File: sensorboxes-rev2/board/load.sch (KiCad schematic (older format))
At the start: 26 parts

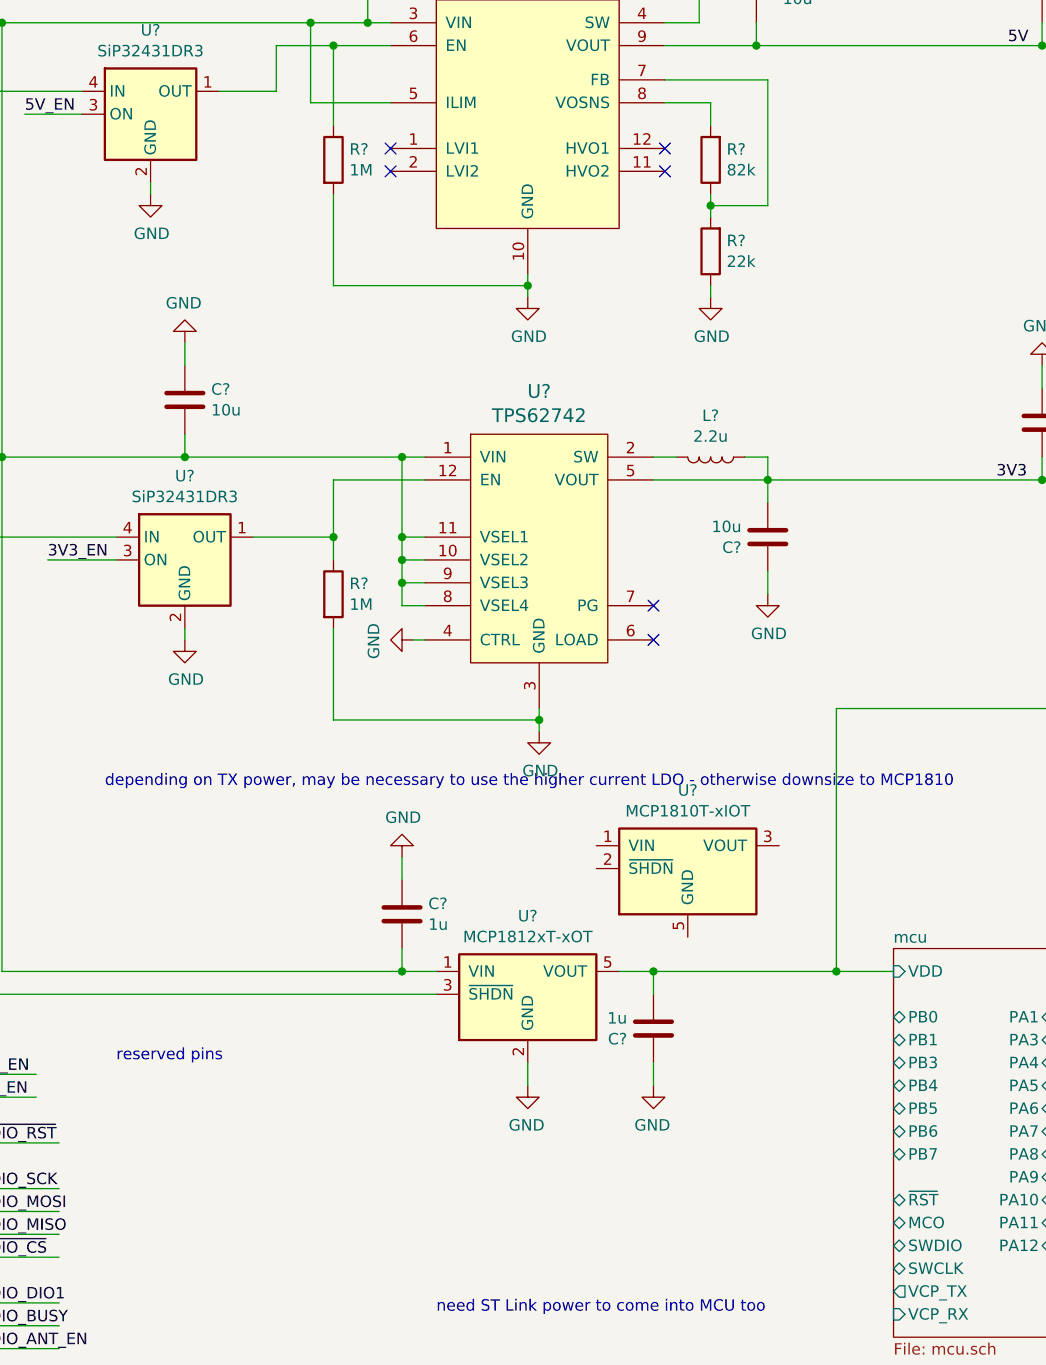
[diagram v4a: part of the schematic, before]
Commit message: exposing pins for mcu, added part values for RF section
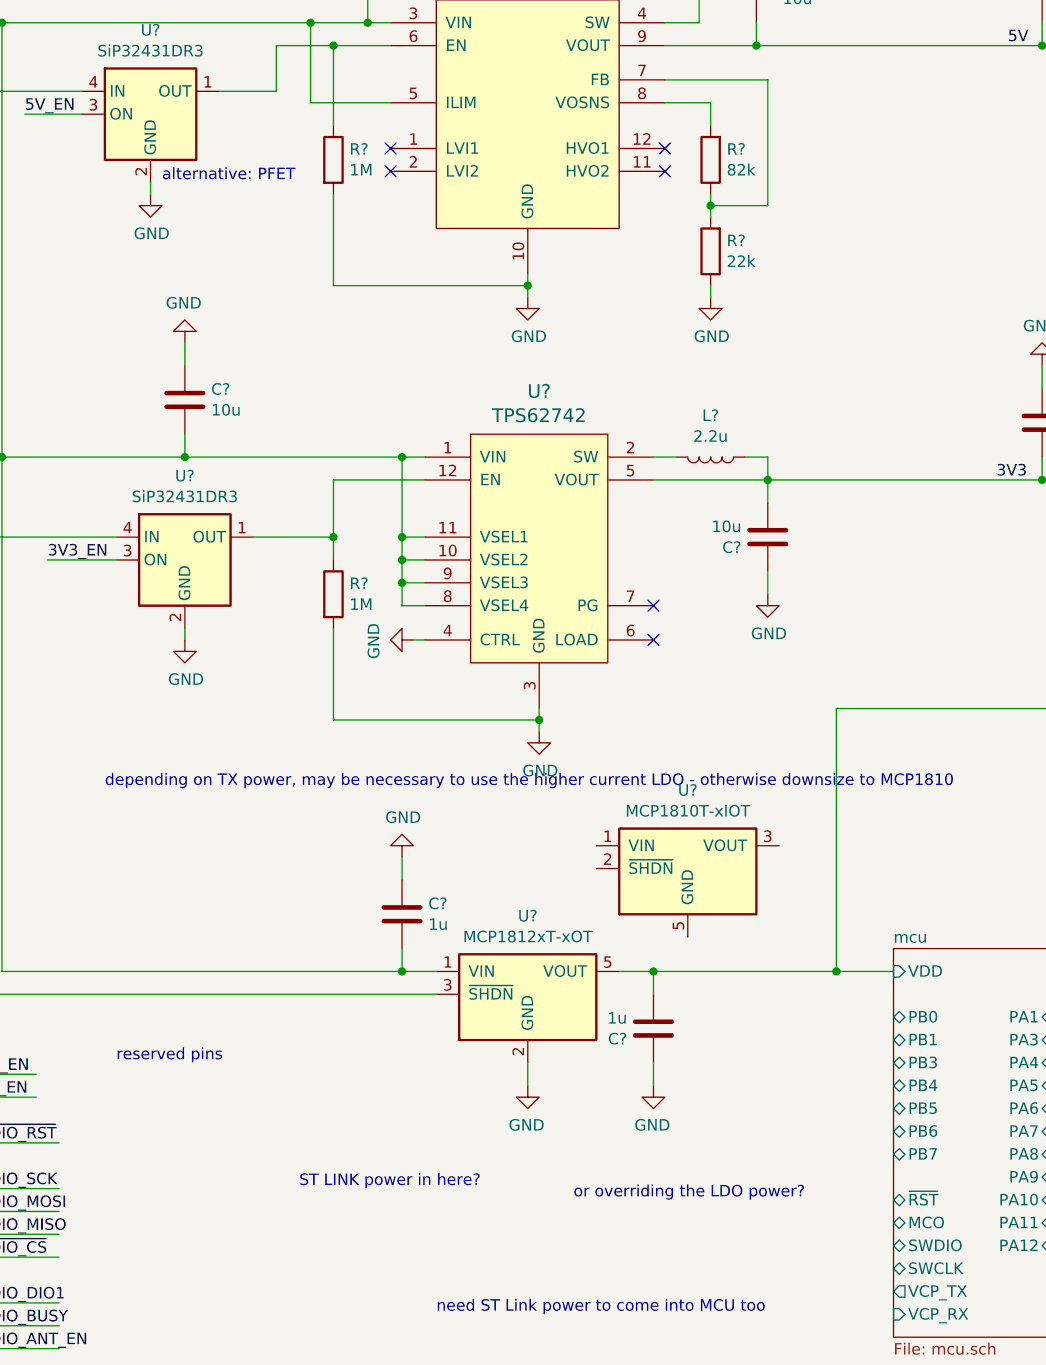
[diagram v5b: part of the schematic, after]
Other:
- note added: "ST LINK power in here?"
- note added: "alternative: PFET"
- note added: "or overriding the LDO power?"
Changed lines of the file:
@@
 Wire Wire Line
 	1300 7600 1700 7600
+Text Notes 2150 2500 0    50   ~ 0
+alternative: PFET
+Text Notes 2750 6900 0    50   ~ 0
+ST LINK power in here?
+Text Notes 3950 6950 0    50   ~ 0
+or overriding the LDO power?
 $EndSCHEMATC

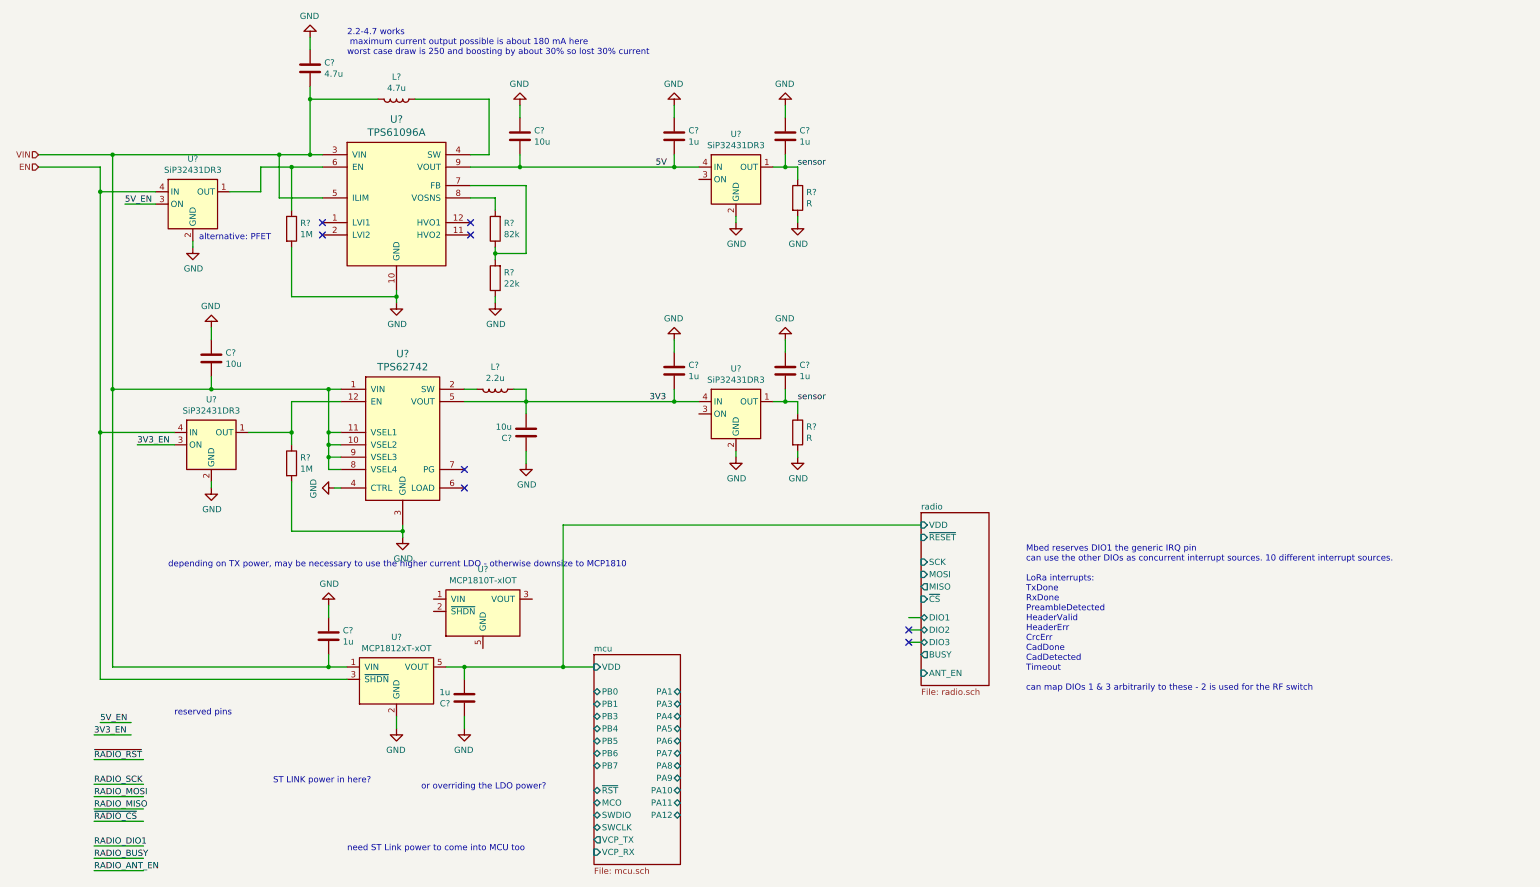
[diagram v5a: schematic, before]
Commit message: some preliminary power figure estimation
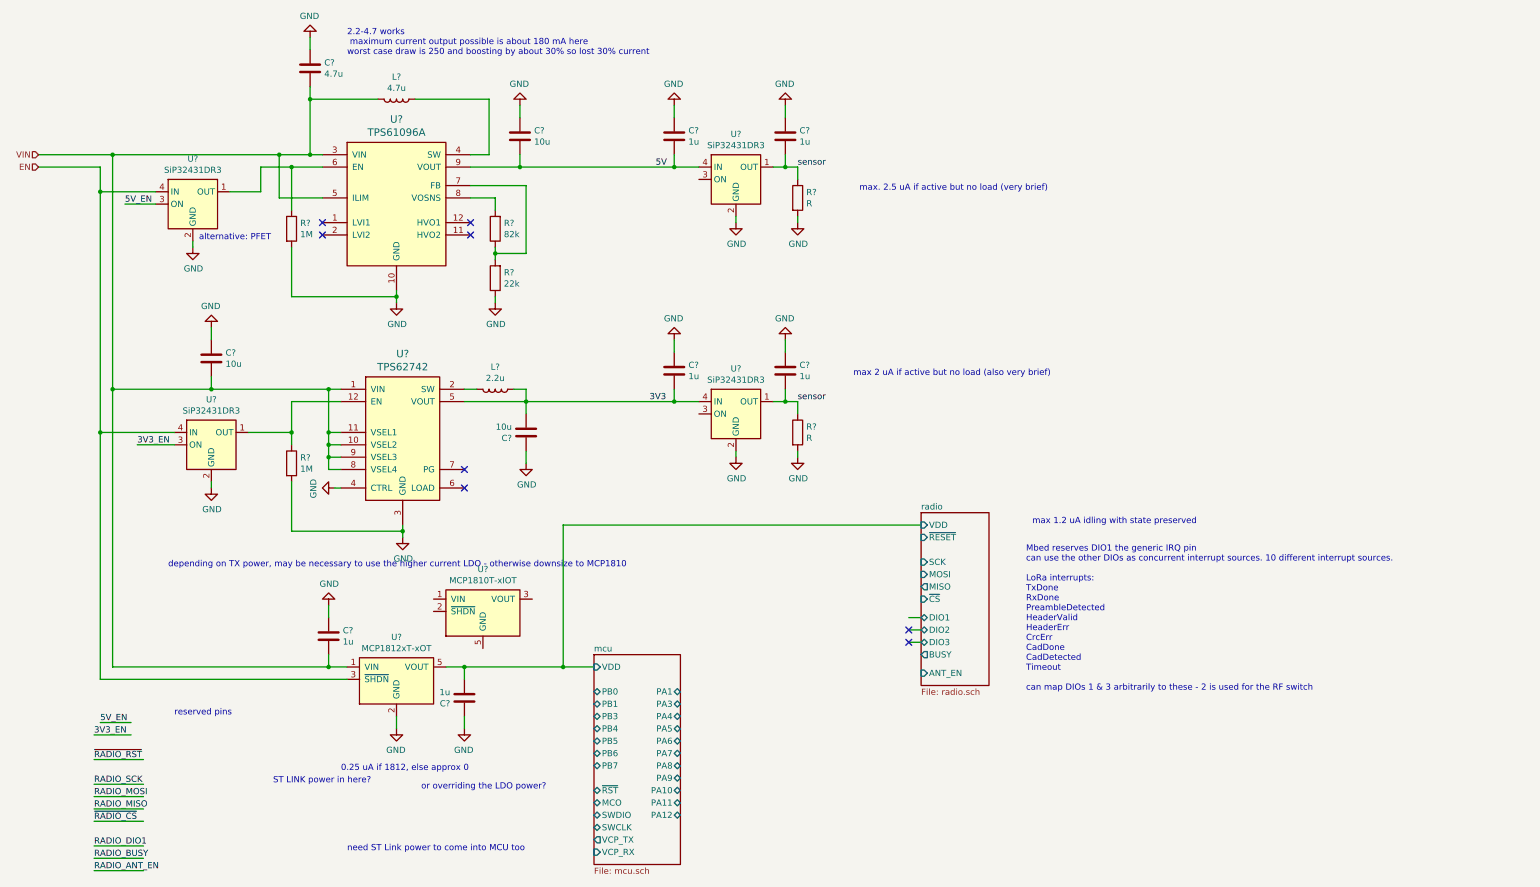
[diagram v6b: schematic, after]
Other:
- note added: "0.25 uA if 1812, else approx 0"
- note added: "max 1.2 uA idling with state preserved"
- note added: "max 2 uA if active but no load (also very brief)"
- note added: "max. 2.5 uA if active but no load (very brief)"
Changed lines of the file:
@@
 Text Notes 3950 6950 0    50   ~ 0
 or overriding the LDO power?
+Text Notes 7500 2100 0    50   ~ 0
+max. 2.5 uA if active but no load (very brief)
+Text Notes 7450 3600 0    50   ~ 0
+max 2 uA if active but no load (also very brief)
+Text Notes 3300 6800 0    50   ~ 0
+0.25 uA if 1812, else approx 0
+Text Notes 8900 4800 0    50   ~ 0
+max 1.2 uA idling with state preserved
 $EndSCHEMATC
